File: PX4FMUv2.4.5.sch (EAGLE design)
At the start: 292 parts, among them J201 DF13C-6P-1.25V, J202 DF13C-6P-1.25V, J203 DF13C-6P-1.25V, J204 DF13C-6P-1.25V, J301 47346-0001, J302 DF13C-4P-1.25V, J401 DF13C-4P-1.25V, J402 DF13C-3P-1.25V, J403 DF13C-7P-1.25V, J404 DF13C-5P-1.25V, J405 DF13C-4P-1.25V, J601 DF13C-6P-1.25V, J701 DF13C-2P-1.25V, J702 DF13C-3P-1.25V, J801 JST-ZH-3, J901 HEADER-3X163X16RA, M3_MOUNT1101 MOUNT-HOLE3.1MM, M3_MOUNT1102 MOUNT-HOLE3.1MM, M3_MOUNT1103 MOUNT-HOLE3.1MM, M3_MOUNT1104 MOUNT-HOLE3.1MM, Q601 MMBT3906LT1SMD, U1001 BQ24313, U1002 MIC5332, U101 STM32F4X7VX, U102 FM25V01, U1101 LTC4417, U1102 NTHD4102PT1G, U1103 NTHD4102PT1G, U1104 NTHD4102PT1G, U201 TXS0108QFN20, U202 TXS0108QFN20, U301 2908-05WB-MG, U302 NUF2042XV6, U401 MAX3051, U501 L3GD20, U502 L3GD20H, U504 LSM303D, U505 MPU-6000, U506 MS5611-01BA, U601 BQ24315, U602 BQ24315, U603 MIC5332, U701 TCA62724FMG, U702 LT3469, U703 LRTB GFTG-T7AW-1+V7A7-29+R5T9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, U801 STM32F10XCXT6, U901 TXS0108QFN20, U902 TXS0108QFN20, U903 74LVC2G240, X101 3.2x2.5 mm / 24 MHz / 15 ppm, X503 0512811094, X801 3.2x2.5 mm / 24 MHz / 15 ppm

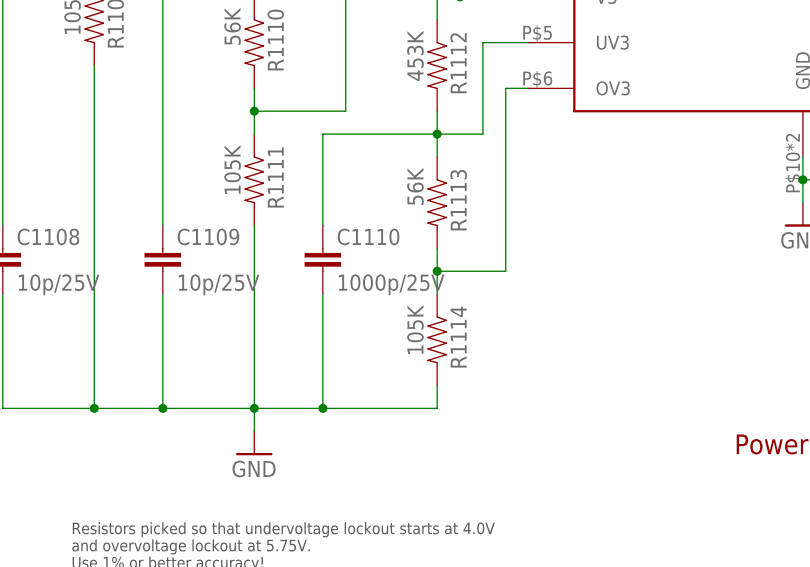
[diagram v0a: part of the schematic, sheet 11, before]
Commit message: FMU v2.4.5 sch mistake fix - C1110 to 10p
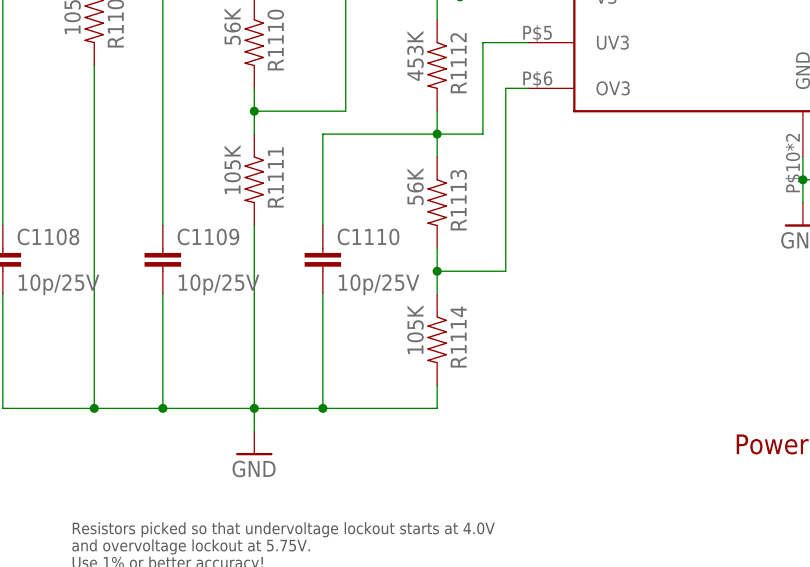
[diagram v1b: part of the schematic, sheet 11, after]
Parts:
- C1110: value 1000p/25V -> 10p/25V; PARTNO GRM1555C1E102JA01D -> C0402C100J3GACTU
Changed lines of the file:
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@@
 <?xml version="1.0" encoding="utf-8"?>
 <!DOCTYPE eagle SYSTEM "eagle.dtd">
-<eagle version="6.5.0">
+<eagle version="7.1.0">
 <drawing>
 <settings>
@@
 <attribute name="PARTNO" value="C0402C100J3GACTU"/>
 </part>
-<part name="C1110" library="pixhawk2" deviceset="CAP" device="0402" value="1000p/25V">
-<attribute name="PARTNO" value="GRM1555C1E102JA01D"/>
+<part name="C1110" library="pixhawk2" deviceset="CAP" device="0402" value="10p/25V">
+<attribute name="PARTNO" value="C0402C100J3GACTU"/>
 </part>
 <part name="C615" library="pixhawk2" deviceset="CAP" device="0402" value="0u1">
